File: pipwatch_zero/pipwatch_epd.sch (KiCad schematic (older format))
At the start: 18 parts, among them Q301 Si1304BDL, X301 MOLEX_FPC_RCPT_24POS

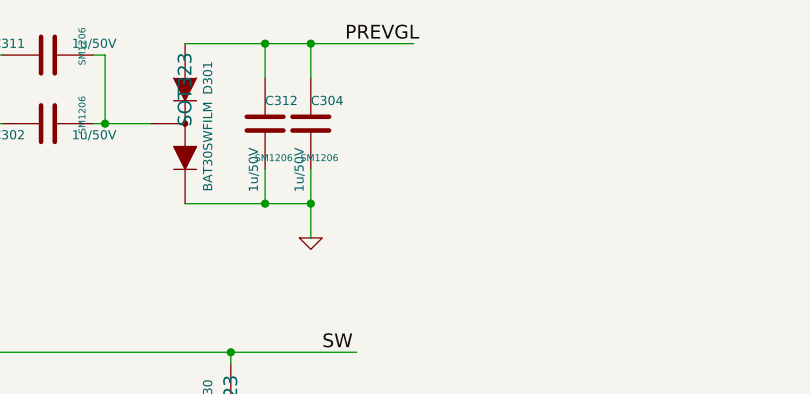
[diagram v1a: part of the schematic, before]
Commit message: sw pipwatch_zero_rtos_u8g_epd_btm; somewhat working, bugs in hw
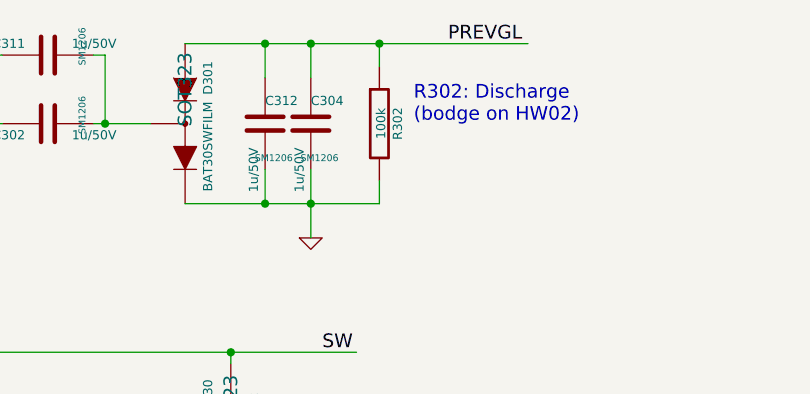
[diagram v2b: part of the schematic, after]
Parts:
- added R302: 100k, ~, symbol R
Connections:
- wire segments 70 -> 72
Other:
- note added: "R302: Discharge\n(bodge on HW02)"
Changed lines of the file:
@@
 Sheet 3 5
 Title ""
-Date "3 sep 2014"
+Date "14 sep 2014"
 Rev "HW02"
 Comp ""
@@
 EPD_SDA
 $Comp
-L 3V3 #PWR09
+L 3V3 #PWR308
 U 1 1 53ED1F53
 P 9100 3800
-F 0 "#PWR09" H 9100 3900 40  0001 C CNN
+F 0 "#PWR308" H 9100 3900 40  0001 C CNN
 F 1 "3V3" H 9100 3925 40  0000 C CNN
 F 2 "" H 9100 3800 60  0000 C CNN
@@
 $EndComp
 $Comp
-L GND #PWR010
+L GND #PWR307
 U 1 1 53ED1F83
 P 8250 2700
-F 0 "#PWR010" H 8250 2700 30  0001 C CNN
+F 0 "#PWR307" H 8250 2700 30  0001 C CNN
 F 1 "GND" H 8250 2630 30  0001 C CNN
 F 2 "" H 8250 2700 60  0000 C CNN
@@
 $EndComp
 $Comp
-L GND #PWR011
+L GND #PWR309
 U 1 1 53ED1F92
 P 9150 3950
-F 0 "#PWR011" H 9150 3950 30  0001 C CNN
+F 0 "#PWR309" H 9150 3950 30  0001 C CNN
 F 1 "GND" H 9150 3880 30  0001 C CNN
 F 2 "" H 9150 3950 60  0000 C CNN
@@
 VCOM
 $Comp
-L GND #PWR012
+L GND #PWR306
 U 1 1 53ED210B
 P 8150 4700
-F 0 "#PWR012" H 8150 4700 30  0001 C CNN
+F 0 "#PWR306" H 8150 4700 30  0001 C CNN
 F 1 "GND" H 8150 4630 30  0001 C CNN
 F 2 "" H 8150 4700 60  0000 C CNN
@@
 $EndComp
 $Comp
-L GND #PWR013
+L GND #PWR303
 U 1 1 53ED2562
 P 3850 4200
-F 0 "#PWR013" H 3850 4200 30  0001 C CNN
+F 0 "#PWR303" H 3850 4200 30  0001 C CNN
 F 1 "GND" H 3850 4130 30  0001 C CNN
 F 2 "" H 3850 4200 60  0000 C CNN
@@
 $EndComp
 $Comp
-L GND #PWR014
+L GND #PWR302
 U 1 1 53ED2661
 P 2550 3400
-F 0 "#PWR014" H 2550 3400 30  0001 C CNN
+F 0 "#PWR302" H 2550 3400 30  0001 C CNN
 F 1 "GND" H 2550 3330 30  0001 C CNN
 F 2 "" H 2550 3400 60  0000 C CNN
@@
 $EndComp
 $Comp
-L 3V3 #PWR015
+L 3V3 #PWR301
 U 1 1 53ED26E9
 P 2550 2600
-F 0 "#PWR015" H 2550 2700 40  0001 C CNN
+F 0 "#PWR301" H 2550 2700 40  0001 C CNN
 F 1 "3V3" H 2550 2725 40  0000 C CNN
 F 2 "" H 2550 2600 60  0000 C CNN
@@
 $EndComp
 $Comp
-L GND #PWR016
+L GND #PWR304
 U 1 1 53ED27DC
 P 5050 4200
-F 0 "#PWR016" H 5050 4200 30  0001 C CNN
+F 0 "#PWR304" H 5050 4200 30  0001 C CNN
 F 1 "GND" H 5050 4130 30  0001 C CNN
 F 2 "" H 5050 4200 60  0000 C CNN
@@
 $EndComp
 $Comp
-L GND #PWR017
+L GND #PWR305
 U 1 1 53ED2B80
 P 5400 2300
-F 0 "#PWR017" H 5400 2300 30  0001 C CNN
+F 0 "#PWR305" H 5400 2300 30  0001 C CNN
 F 1 "GND" H 5400 2230 30  0001 C CNN
 F 2 "" H 5400 2300 60  0000 C CNN
@@
 	1    0    0    -1
 $EndComp
-Text Label 5550 1450 0    60   ~ 0
+Text Label 6000 1450 0    60   ~ 0
 PREVGL
 $Comp
@@
 	4450 1800 4700 1800
 Wire Wire Line
-	4850 1450 5850 1450
+	4850 1450 6350 1450
 Wire Wire Line
 	5400 1450 5400 1600
 Wire Wire Line
-	4850 2150 5400 2150
+	4850 2150 5700 2150
 Wire Wire Line
 	5400 2000 5400 2300
@@
 	5200 2000 5200 2150
 Connection ~ 5200 2150
+$Comp
+L R R302
+U 1 1 5415CB7C
+P 5700 1800
+F 0 "R302" V 5780 1800 40  0000 C CNN
+F 1 "100k" V 5707 1801 40  0000 C CNN
+F 2 "~" V 5630 1800 30  0000 C CNN
+F 3 "~" H 5700 1800 30  0000 C CNN
+	1    5700 1800
+	1    0    0    -1
+$EndComp
+Wire Wire Line
+	5700 1550 5700 1450
+Connection ~ 5700 1450
+Wire Wire Line
+	5700 2150 5700 2050
+Text Notes 5850 1800 0    60   ~ 0
+R302: Discharge\n(bodge on HW02)
 $EndSCHEMATC
